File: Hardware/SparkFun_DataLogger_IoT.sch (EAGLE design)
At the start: 99 parts, among them J10 QWIIC_RIGHT_ANGLE, J3 MICRO-SD-PUSH-PUSH-EXT-PIN, J4 Vertical Qwiic Connector, U1 ESP-WROOM-32E, U10 74HC4066_QUAD_BILATERAL_SWITC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, U2 CH340C, U3 XC6222B331MR-G, U4 MAX17048, U5 MCP73831, U6 XC6222B331MR-G, U9 74HC4066_QUAD_BILATERAL_SWITC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

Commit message: Pre-Design Review updates
Add 9.1k Res for hardware versioning.
Move MEAS to be on grid.
Shuffle diodes around a little.
Move silk to fill gaps.
Change LED bias resistor to meet standards.
Made HW versioning be on A7 to match RTK designs.
Replaced A7 breakout with D5.
Relabeled silk.
Added silk to RGB LED.
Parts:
- removed R20, R21: 100k, SparkFun-Resistors:100KOHM-0402T-1/16W-1%
- R17: value 1M -> 100k; device SparkFun-Resistors:1MOHM-0402T-1/16W-5% -> SparkFun-Resistors:100KOHM-0402T-1/16W-1%
- R6: value 1k -> 2.2k; device SparkFun-Resistors:1KOHM-0402T-1/16W-1% -> SparkFun-Resistors:2.2KOHM-0402T-1/16W-1%
- R9: value 93.1k -> 9.1K; device SparkFun-Resistors:93.1KOHM-0402-1/16W-1%(93.1KOHM) -> RA_RGB:9.1KOHM-0402T-1/16W-1%
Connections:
- removed net ESP34/A6: R17.2, R9.1, U1.IA34
- new net ESP5: J8.5, U1.CS3/IO5
- net 3.3V: no longer R20.2, R21.2
- net ESP18/SCK: no longer R20.1
- net ESP23/PICO: no longer R21.1
- net ESP35/A7: now also R17.2, R9.1; no longer J8.5
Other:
- note added: "v10 should read ~0.275V"
- note removed: "v10 should read ~0.281V"
- moved on the sheet: J6, R22

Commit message: Post design review updates.
Change BO silk for D5.
Remove unused PURs.
Clean up wire stubs.
Remove GND guard trace.
Add GND vias near switching vias.
Renumber Schematic.
Repanelize and pull together outer border.
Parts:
- removed C28, C29, C30: 2.2uF, SparkFun-Capacitors:2.2UF-0402_TIGHT-10V-10%-X5R
- removed C31: 0.1uF, SparkFun-Capacitors:0.1UF-0402T-6.3V-10%-X7R
- removed J10: QWIIC_RIGHT_ANGLE, SparkFun-Connectors:QWIIC_CONNECTORJS-1MM
- removed R22: 10k, SparkFun-Resistors:10KOHM-0402T-1/16W-1%
- removed U10, U9: 74HC4066_QUAD_BILATERAL_SWITCH_QFN, SparkFun-IC-Logic:74HC4066_QUAD_BILATERAL_SWITCH_QFN
- added C21, C22, C24: 2.2uF, SparkFun-Capacitors:2.2UF-0402_TIGHT-10V-10%-X5R
- added C23: 0.1uF, SparkFun-Capacitors:0.1UF-0402T-6.3V-10%-X7R
- added J9: (no value), SparkFun-Connectors:JST_2MM_MALE
- added R18: 2.2k, SparkFun-Resistors:2.2KOHM-0402T-1/16W-1%
- added U7: MAX17048, SparkFun-IC-Power:MAX17048DFN8
- added U8: XC6222B331MR-G, SparkFun-IC-Power:XC6222B331MR-G
- C10, C14, C27, C5: value 2.2uF -> 0.1uF; device SparkFun-Capacitors:2.2UF-0402_TIGHT-10V-10%-X5R -> SparkFun-Capacitors:0.1UF-0402T-6.3V-10%-X7R
- C12: value 2.2uF -> 10nF; device SparkFun-Capacitors:2.2UF-0402_TIGHT-10V-10%-X5R -> SparkFun-Capacitors:10NF-0402T-25V-10%-X7R-WE
- C13, C15, C17, C19: value 0.1uF -> 2.2uF; device SparkFun-Capacitors:0.1UF-0402T-6.3V-10%-X7R -> SparkFun-Capacitors:2.2UF-0402_TIGHT-10V-10%-X5R
- C4: value 10nF -> 2.2uF; device SparkFun-Capacitors:10NF-0402T-25V-10%-X7R-WE -> SparkFun-Capacitors:2.2UF-0402_TIGHT-10V-10%-X5R
- D1: value BLUE -> 3A/10V/280mV; device SparkFun-LED:LED-BLUE0603 -> SparkFun-DiscreteSemi:DIODE-SCHOTTKY-BAT60A
- D2: value B3DQ3BRG -> 3A/10V/280mV; device RA_RGB:B3DQ3BRG -> SparkFun-DiscreteSemi:DIODE-SCHOTTKY-BAT60A
- D3: value Yellow -> 3A/10V/280mV; device SparkFun-LED:LED-YELLOW0603 -> SparkFun-DiscreteSemi:DIODE-SCHOTTKY-BAT60A
- D4: value 3A/10V/280mV -> TVS; device SparkFun-DiscreteSemi:DIODE-SCHOTTKY-BAT60A -> SparkFun-DiscreteSemi:DIODE_TVS
- D5: value 3A/10V/280mV -> Yellow; device SparkFun-DiscreteSemi:DIODE-SCHOTTKY-BAT60A -> SparkFun-LED:LED-YELLOW0603
- D6: value 3A/10V/280mV -> B3DQ3BRG; device SparkFun-DiscreteSemi:DIODE-SCHOTTKY-BAT60A -> RA_RGB:B3DQ3BRG
- D7: value TVS -> BLUE; device SparkFun-DiscreteSemi:DIODE_TVS -> SparkFun-LED:LED-BLUE0603
- J1: value (none) -> MICRO-SD-PUSH-PUSH-EXT-PIN; device SparkFun-Connectors:USB_C_4-LAYER_PADS -> SparkFun-Connectors:MICRO-SD-PUSH-PUSH-EXT-PIN
- J2: device SparkFun-Connectors:JST_2MM_MALE -> SparkFun-Connectors:CONN_06NO_SILK_NO_POP
- J3: value MICRO-SD-PUSH-PUSH-EXT-PIN -> QWIIC_RIGHT_ANGLE; device SparkFun-Connectors:MICRO-SD-PUSH-PUSH-EXT-PIN -> SparkFun-Connectors:QWIIC_CONNECTORJS-1MM
- J4: value Vertical Qwiic Connector -> (none); device SparkFun-Connectors:QWIIC_CONNECTOR -> SparkFun-Connectors:USB_C_4-LAYER_PADS
- J5: device SparkFun-Connectors:I2C_STANDARD_NO_SILK -> SparkFun-Connectors:CONN_041X04_NO_SILK_NO_POP
- J6: value (none) -> Vertical Qwiic Connector; device SparkFun-Connectors:CONN_041X04_NO_SILK_NO_POP -> SparkFun-Connectors:QWIIC_CONNECTOR
- J7: device SparkFun-Connectors:CONN_06NO_SILK_NO_POP -> SparkFun-Connectors:CONN_09NO_SILK
- J8: device SparkFun-Connectors:CONN_09NO_SILK -> SparkFun-Connectors:I2C_STANDARD_NO_SILK
- LOGO1: value SPECIAL_INSTRUCTIONS-ORDERING -> SFE_LOGO_NAME.2_INCH; device SparkFun-Aesthetics:SPECIAL_INSTRUCTIONS-ORDERING -> SparkFun-Aesthetics:SFE_LOGO_NAME.2_INCH
- LOGO3: value QWIIC_LOGO_6MM -> SPECIAL_INSTRUCTIONS-ORDERING; device SparkFun-Aesthetics:QWIIC_LOGO_6MM -> SparkFun-Aesthetics:SPECIAL_INSTRUCTIONS-ORDERING
- LOGO4: value OSHW-LOGOS -> QWIIC_LOGO_6MM; device SparkFun-Aesthetics:OSHW-LOGOS -> SparkFun-Aesthetics:QWIIC_LOGO_6MM
- LOGO5: value SFE_LOGO_NAME.2_INCH -> OSHW-LOGOS; device SparkFun-Aesthetics:SFE_LOGO_NAME.2_INCH -> SparkFun-Aesthetics:OSHW-LOGOS
- R1, R2: value 5.1k -> 10k; device SparkFun-Resistors:5.1KOHM-0402T-1/16W-1% -> SparkFun-Resistors:10KOHM-0402T-1/16W-1%
- R13: value 10k -> 1k; device SparkFun-Resistors:10KOHM-0402T-1/16W-1% -> SparkFun-Resistors:1KOHM-0402T-1/16W-1%
- R14: value 10k -> 2.0K; device SparkFun-Resistors:10KOHM-0402T-1/16W-1% -> SparkFun-Resistors:2.0KOHM-0402T-1/16W-1%
- R15: value 10k -> 2.2k; device SparkFun-Resistors:10KOHM-0402T-1/16W-1% -> SparkFun-Resistors:2.2KOHM-0402T-1/16W-1%
- R16: value 2.2k -> 100k; device SparkFun-Resistors:2.2KOHM-0402T-1/16W-1% -> SparkFun-Resistors:100KOHM-0402T-1/16W-1%
- R17: value 100k -> 9.1K; device SparkFun-Resistors:100KOHM-0402T-1/16W-1% -> RA_RGB:9.1KOHM-0402T-1/16W-1%
- R6: value 2.2k -> 10k; device SparkFun-Resistors:2.2KOHM-0402T-1/16W-1% -> SparkFun-Resistors:10KOHM-0402T-1/16W-1%
- R7: value 2.0K -> 10k; device SparkFun-Resistors:2.0KOHM-0402T-1/16W-1% -> SparkFun-Resistors:10KOHM-0402T-1/16W-1%
- R8: value 1k -> 5.1k; device SparkFun-Resistors:1KOHM-0402T-1/16W-1% -> SparkFun-Resistors:5.1KOHM-0402T-1/16W-1%
- R9: value 9.1K -> 5.1k; device RA_RGB:9.1KOHM-0402T-1/16W-1% -> SparkFun-Resistors:5.1KOHM-0402T-1/16W-1%
- U2: value CH340C -> 74HC4066_QUAD_BILATERAL_SWITCH_QFN; device SparkFun-IC-Comms:CH340C -> SparkFun-IC-Logic:74HC4066_QUAD_BILATERAL_SWITCH_QFN
- U4: value MAX17048 -> CH340C; device SparkFun-IC-Power:MAX17048DFN8 -> SparkFun-IC-Comms:CH340C
- U6: value XC6222B331MR-G -> 74HC4066_QUAD_BILATERAL_SWITCH_QFN; device SparkFun-IC-Power:XC6222B331MR-G -> SparkFun-IC-Logic:74HC4066_QUAD_BILATERAL_SWITCH_QFN
- renumbered LOGO6 to LOGO2, PWREN to TP4, VIN to TP2, VIN1 to TP3
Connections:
- net !RESET!: now also C5.1, J7.9, R1.1, U2.4E; no longer C31.1, J8.9, R3.1, U9.4E
- net 3.3V: now also C11.1, C12.1, C13.1, C17.1, C18.1, C6.1, C7.1, J2.5, R1.2, R10.2, R16.1, U3.OUT, U4.V3, U4.VCC, U6.VCC; no longer C1.1, C15.1, C2.1, C25.1, C26.1, C27.1, C28.1, J7.5, R17.1, R22.2, R3.2, U10.VCC, U2.V3, U6.OUT, U9.VCC
- net 3.3V_SW: now also C1.1, C2.1, C25.1, C26.1, C27.1, C8.1, D6.VCC, J1.VCC, J3.2, J6.2, J8.2, R2.2, R3.2, R4.2, R5.2, R6.2, U8.OUT; no longer C18.1, C19.1, C20.1, C5.1, C6.1, C7.1, D2.VCC, J10.2, J3.VCC, J4.2, J5.2, R10.2, R11.2, R12.2, R13.2, R14.2, U3.OUT
- net 5V: now also D3.A, J2.3; no longer D6.A, J7.3
- net CH340-DTR: now also R11.2, U4.!DTR; no longer R4.2, U2.!DTR
- net CH340-RTS: now also R12.2, U4.!RTS; no longer R5.2, U2.!RTS
- net CH340-RX: now also U4.RXI; no longer U2.RXI
- net CH340-TX: now also U4.TXO; no longer U2.TXO
- net D+: now also J4.D+, U4.UD+; no longer J1.D+, U2.UD+
- net D-: now also J4.D-, U4.UD-; no longer J1.D-, U2.UD-
- net ESP0/!BOOT!: now also J7.8; no longer J8.8
- net ESP12/DAT2: now also U2.2Y; no longer U9.2Y
- net ESP13/DAT3: now also J1.DAT3/!CS!, R2.1; no longer J3.DAT3/!CS!, R14.1
- net ESP14/CLK: now also J1.CLK/SCK; no longer J3.CLK/SCK
- net ESP15/CMD: now also U2.3Y; no longer U9.3Y
- net ESP16/RXD: now also J7.3; no longer J8.3
- net ESP17/TXD: now also J7.4; no longer J8.4
- net ESP18/SCK: now also J5.4; no longer J6.4
- net ESP19/POCI: now also J5.2, R10.1; no longer J6.2, R22.1
- net ESP2/DAT0: now also U2.1Y; no longer U9.1Y
- net ESP21/SDA: now also R15.1, U6.2Y, U7.SDA; no longer R19.1, U10.2Y, U4.SDA
- net ESP22/SCL: now also R18.2, U6.4Y, U7.SCL; no longer R16.2, U10.4Y, U4.SCL
- net ESP23/PICO: now also J5.3; no longer J6.3
- net ESP25/LED: now also J7.2, R19.2; no longer J8.2, R6.2
- net ESP26/RGBLED: now also J7.1; no longer J8.1
- net ESP32/PWREN: now also U2.4Y; no longer U9.4Y
- net ESP33: now also J5.1; no longer J6.1
- net ESP35/A7: now also R16.2, R17.1; no longer R17.2, R9.1
- net ESP36/A0: now also J7.7; no longer J8.7
- net ESP39/A3: now also J7.6; no longer J8.6
- net ESP4/DAT1: now also J1.DAT1, R4.1; no longer J3.DAT1, R12.1
- net ESP5: now also J7.5; no longer J8.5
- net GND: now also C21.2, C22.2, C23.2, C24.2, D4.A, D6.GND, D7.C, J2.2, J2.4, J2.6, J3.1, J4.GND, J6.1, J8.1, J9.-, R14.1, R17.2, R8.1, R9.1, U6.1E, U6.3E, U7.CTG, U7.GND, U7.QSTRT, U8.GND; no longer C28.2, C29.2, C30.2, C31.2, D1.C, D2.GND, D7.A, J10.1, J2.-, J3.GND, J4.1, J5.1, J7.2, J7.4, J7.6, R1.1, R15.1, R2.1, R9.2, U10.1E, U10.3E, U10.GND, U4.CTG, U4.QSTRT, U9.GND
- net N$1: now also J4.CC2, R8.2; no longer J1.CC2, R1.2
- net N$10: now also R13.2; no longer R8.2
- net N$11: now also R14.2; no longer R7.2
- net N$12: now also D6.DI; no longer D2.DI
- net N$13: now also D7.A; no longer D1.A
- net N$16: now also R18.1; no longer R16.1
- net N$17: now also R15.2; no longer R19.2
- net N$2: now also J4.CC1, R9.2; no longer J1.CC1, R2.2
- net N$3: now also D1.C, D2.C, D3.C; no longer D4.C, D5.C, D6.C
- net N$4: now also R12.1; no longer R5.1
- net N$5: now also R11.1; no longer R4.1
- net N$6: now also R19.1; no longer R6.1
- net N$7: now also D6.DO; no longer D2.DO
- net N$8: now also D5.A; no longer D3.A
- net N$9: now also D5.C, R13.1; no longer D3.C, R8.1
- net PWREN: now also R7.2, U2.1E, U2.2E, U2.3E, U2.4Z, U6.2E, U6.4E, U8.EN; no longer R15.2, U10.2E, U10.4E, U3.EN, U9.1E, U9.2E, U9.3E, U9.4Z
- net QWIIC_SCL: now also J3.4, J6.4, J8.4, U6.4Z; no longer J10.4, J4.4, J5.4, U10.4Z
- net QWIIC_SDA: now also J3.3, J6.3, J8.3, U6.2Z; no longer J10.3, J4.3, J5.3, U10.2Z
- net SD_CMD: now also J1.CMD/SDI, R6.1, U2.3Z; no longer J3.CMD/SDI, R10.1, U9.3Z
- net SD_DAT0: now also J1.DAT0/SDO, R5.1, U2.1Z; no longer J3.DAT0/SDO, R11.1, U9.1Z
- net SD_DAT2: now also J1.DAT2, R3.1, U2.2Z; no longer J3.DAT2, R13.1, U9.2Z
- net SHIELD: now also J4.SHLD; no longer J1.SHLD
- net VIN: now also C15.1, C19.1, C21.1, C22.1, C24.1, U3.EN, U8.IN; no longer C12.1, C16.1, C17.1, C29.1, C8.1, U6.EN, U6.IN
- net V_BATT: now also C16.1, C20.1, C23.1, D1.A, J2.1, J9.+, U7.CELL, U7.VDD; no longer C11.1, C13.1, C30.1, D4.A, J2.+, J7.1, U4.CELL, U4.VDD
- net V_USB: now also D2.A, D4.C, J4.VBUS; no longer D5.A, D7.C, J1.VBUS
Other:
- note added: "TP2"
- note added: "TP3"
- note added: "TP4"
- note removed: "Close jumper to connect INT to ESP35"
- moved on the sheet: C1, C10, C11, C12, C13, C14, C15, C16, C17, C18, C19, C2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

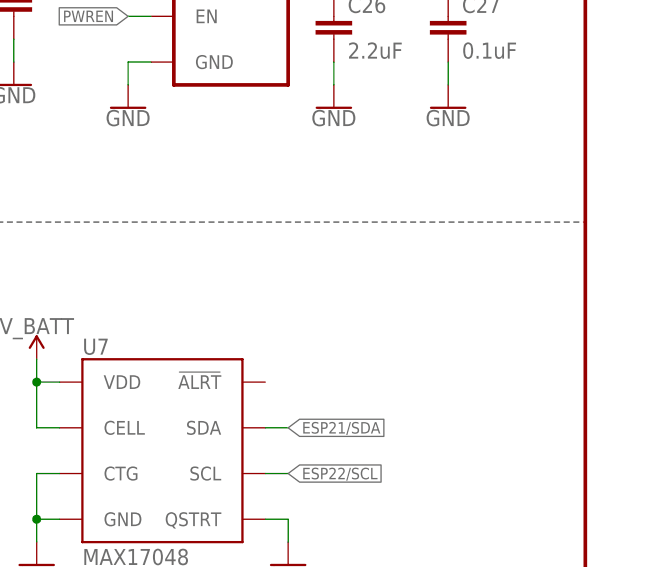
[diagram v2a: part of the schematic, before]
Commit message: Added Fuel Gauge I2C address.
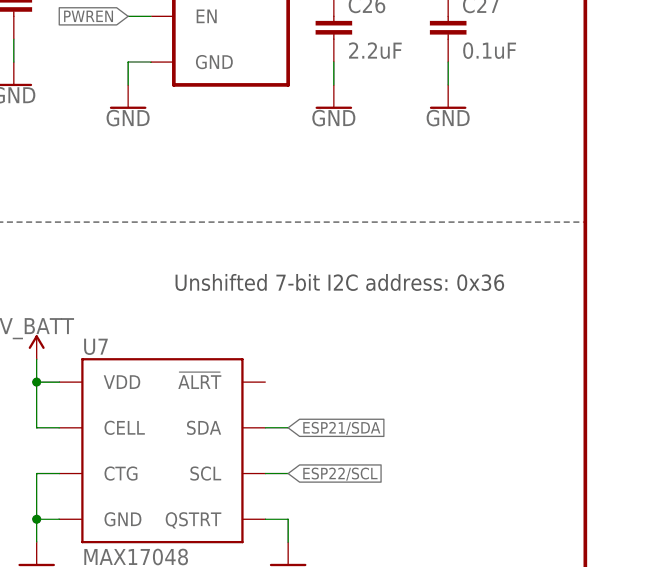
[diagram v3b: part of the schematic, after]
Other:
- note added: "Unshifted 7-bit I2C address: 0x36"
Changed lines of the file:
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@@
 <text x="264.16" y="147.32" size="1.778" layer="95" font="vector">TP3</text>
 <text x="81.28" y="43.18" size="1.778" layer="95" font="vector">TP4</text>
+<text x="386.08" y="167.64" size="1.778" layer="97" font="vector">Unshifted 7-bit I2C address: 0x36</text>
 </plain>
 <instances>

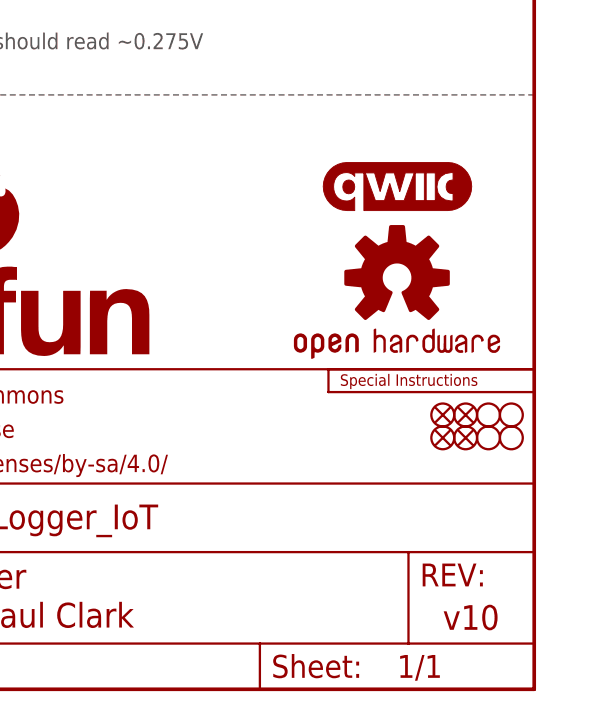
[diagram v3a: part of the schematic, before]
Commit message: Update for v11 PCB
Removed OSHW logo.
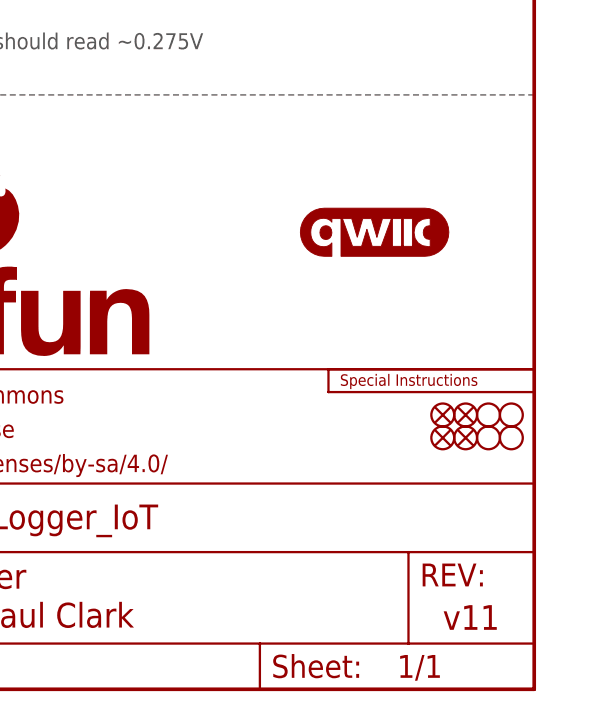
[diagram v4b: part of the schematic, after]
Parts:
- removed LOGO5: OSHW-LOGOS, SparkFun-Aesthetics:OSHW-LOGOS
- FRAME1: REV v10 -> v11
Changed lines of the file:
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@@
 <part name="FRAME1" library="SparkFun-Aesthetics" deviceset="FRAME-LEDGER" device="">
 <attribute name="DESIGNER" value="Alex Brudner"/>
-<attribute name="REV" value="v10"/>
+<attribute name="REV" value="v11"/>
 </part>
 <part name="LOGO3" library="SparkFun-Aesthetics" deviceset="SPECIAL_INSTRUCTIONS" device="-ORDERING"/>
@@
 <part name="H1" library="SparkFun-Hardware" deviceset="STAND-OFF" device="TIGHT"/>
 <part name="LOGO4" library="SparkFun-Aesthetics" deviceset="QWIIC_LOGO" device="_6MM" value="QWIIC_LOGO_6MM"/>
-<part name="LOGO5" library="SparkFun-Aesthetics" deviceset="OSHW-LOGO" device="S" value="OSHW-LOGOS"/>
 <part name="SUPPLY7" library="SparkFun-PowerSymbols" deviceset="V_USB" device=""/>
 <part name="GND10" library="SparkFun-PowerSymbols" deviceset="GND" device=""/>
@@
 </instance>
 <instance part="H1" gate="G$1" x="426.72" y="30.48" smashed="yes"/>
-<instance part="LOGO4" gate="G$1" x="416.56" y="55.88" smashed="yes"/>
-<instance part="LOGO5" gate="G$1" x="416.56" y="45.72" smashed="yes"/>
+<instance part="LOGO4" gate="G$1" x="414.02" y="50.8" smashed="yes"/>
 <instance part="SUPPLY7" gate="G$1" x="149.86" y="228.6" smashed="yes">
 <attribute name="VALUE" x="149.86" y="231.394" size="1.778" layer="96" align="bottom-center"/>

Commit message: Condensed Schematic.
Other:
- note removed: "HW Versioning"
- note removed: "v10 should read ~0.275V"
- moved on the sheet: R16, R17
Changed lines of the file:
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@@
 <text x="106.68" y="35.56" size="2.54" layer="94" font="vector">Qwiic Connectors</text>
 <wire x1="99.06" y1="43.18" x2="99.06" y2="0" width="0.1524" layer="97" style="longdash"/>
-<wire x1="330.2" y1="35.56" x2="330.2" y2="66.04" width="0.1524" layer="97" style="longdash"/>
-<wire x1="330.2" y1="66.04" x2="330.2" y2="106.68" width="0.1524" layer="97" style="longdash"/>
+<wire x1="330.2" y1="35.56" x2="330.2" y2="106.68" width="0.1524" layer="97" style="longdash"/>
 <wire x1="223.52" y1="106.68" x2="223.52" y2="43.18" width="0.1524" layer="97" style="longdash"/>
 <wire x1="223.52" y1="43.18" x2="223.52" y2="0" width="0.1524" layer="97" style="longdash"/>
-<text x="337.82" y="99.06" size="2.54" layer="94" font="vector">HW Versioning</text>
-<wire x1="431.8" y1="66.04" x2="330.2" y2="66.04" width="0.1524" layer="97" style="longdash"/>
-<text x="381" y="71.12" size="1.778" layer="97" font="vector" align="bottom-center">v10 should read ~0.275V</text>
 <text x="165.1" y="142.24" size="1.778" layer="95" font="vector">TP2</text>
 <text x="264.16" y="147.32" size="1.778" layer="95" font="vector">TP3</text>
@@
 </instance>
 <instance part="H1" gate="G$1" x="426.72" y="30.48" smashed="yes"/>
-<instance part="LOGO4" gate="G$1" x="414.02" y="50.8" smashed="yes"/>
+<instance part="LOGO4" gate="G$1" x="414.02" y="43.18" smashed="yes"/>
 <instance part="SUPPLY7" gate="G$1" x="149.86" y="228.6" smashed="yes">
 <attribute name="VALUE" x="149.86" y="231.394" size="1.778" layer="96" align="bottom-center"/>
@@
 <instance part="LOGO1" gate="G$1" x="332.74" y="33.02" smashed="yes"/>
 <instance part="LOGO2" gate="G$1" x="365.76" y="44.45" smashed="yes"/>
-<instance part="R17" gate="G$1" x="388.62" y="86.36" smashed="yes">
-<attribute name="NAME" x="388.62" y="87.884" size="1.778" layer="95" font="vector" align="bottom-center"/>
-<attribute name="VALUE" x="388.62" y="84.836" size="1.778" layer="96" font="vector" align="top-center"/>
-</instance>
-<instance part="R16" gate="G$1" x="373.38" y="86.36" smashed="yes">
-<attribute name="NAME" x="373.38" y="87.884" size="1.778" layer="95" font="vector" align="bottom-center"/>
-<attribute name="VALUE" x="373.38" y="84.836" size="1.778" layer="96" font="vector" align="top-center"/>
-</instance>
-<instance part="SUPPLY31" gate="G$1" x="365.76" y="88.9" smashed="yes">
-<attribute name="VALUE" x="365.76" y="91.694" size="1.778" layer="96" align="bottom-center"/>
-</instance>
-<instance part="GND36" gate="1" x="396.24" y="81.28" smashed="yes">
-<attribute name="VALUE" x="396.24" y="81.026" size="1.778" layer="96" font="vector" align="top-center"/>
+<instance part="R17" gate="G$1" x="86.36" y="193.04" smashed="yes" rot="R270">
+<attribute name="NAME" x="87.884" y="193.04" size="1.778" layer="95" font="vector" rot="R270" align="bottom-center"/>
+<attribute name="VALUE" x="92.456" y="193.04" size="1.778" layer="96" font="vector" rot="R270" align="top-center"/>
+</instance>
+<instance part="R16" gate="G$1" x="86.36" y="208.28" smashed="yes" rot="R270">
+<attribute name="NAME" x="87.884" y="208.28" size="1.778" layer="95" font="vector" rot="R270" align="bottom-center"/>
+<attribute name="VALUE" x="92.456" y="208.28" size="1.778" layer="96" font="vector" rot="R270" align="top-center"/>
+</instance>
+<instance part="SUPPLY31" gate="G$1" x="86.36" y="215.9" smashed="yes">
+<attribute name="VALUE" x="86.36" y="218.694" size="1.778" layer="96" align="bottom-center"/>
+</instance>
+<instance part="GND36" gate="1" x="86.36" y="182.88" smashed="yes">
+<attribute name="VALUE" x="86.36" y="182.626" size="1.778" layer="96" font="vector" align="top-center"/>
 </instance>
 <instance part="MEAS" gate="JP1" x="139.7" y="139.7" smashed="yes">
@@
 </segment>
 <segment>
-<wire x1="393.7" y1="86.36" x2="396.24" y2="86.36" width="0.1524" layer="91"/>
 <pinref part="GND36" gate="1" pin="GND"/>
-<wire x1="396.24" y1="86.36" x2="396.24" y2="83.82" width="0.1524" layer="91"/>
+<wire x1="86.36" y1="187.96" x2="86.36" y2="185.42" width="0.1524" layer="91"/>
 <pinref part="R17" gate="G$1" pin="2"/>
 </segment>
@@
 <segment>
 <pinref part="SUPPLY31" gate="G$1" pin="3.3V"/>
-<wire x1="365.76" y1="86.36" x2="365.76" y2="88.9" width="0.1524" layer="91"/>
 <pinref part="R16" gate="G$1" pin="1"/>
-<wire x1="368.3" y1="86.36" x2="365.76" y2="86.36" width="0.1524" layer="91" style="longdash"/>
+<wire x1="86.36" y1="213.36" x2="86.36" y2="215.9" width="0.1524" layer="91"/>
 </segment>
 </net>
@@
 <net name="ESP35/A7" class="0">
 <segment>
-<pinref part="U1" gate="U1" pin="IA35"/>
-<wire x1="66.04" y1="200.66" x2="68.58" y2="200.66" width="0.1524" layer="91"/>
-<label x="68.58" y="200.66" size="1.27" layer="95" font="vector" xref="yes"/>
-</segment>
-<segment>
 <pinref part="R17" gate="G$1" pin="1"/>
 <pinref part="R16" gate="G$1" pin="2"/>
-<wire x1="383.54" y1="86.36" x2="381" y2="86.36" width="0.1524" layer="91"/>
-<wire x1="381" y1="86.36" x2="378.46" y2="86.36" width="0.1524" layer="91"/>
-<wire x1="381" y1="86.36" x2="381" y2="78.74" width="0.1524" layer="91"/>
-<wire x1="381" y1="78.74" x2="378.46" y2="78.74" width="0.1524" layer="91"/>
-<junction x="381" y="86.36"/>
-<label x="378.46" y="78.74" size="1.27" layer="95" font="vector" rot="R180" xref="yes"/>
-</segment>
-</net>
+<wire x1="86.36" y1="198.12" x2="86.36" y2="200.66" width="0.1524" layer="91"/>
+<wire x1="86.36" y1="200.66" x2="86.36" y2="203.2" width="0.1524" layer="91"/>
+<wire x1="86.36" y1="200.66" x2="81.28" y2="200.66" width="0.1524" layer="91"/>
+<wire x1="81.28" y1="200.66" x2="81.28" y2="198.12" width="0.1524" layer="91"/>
+<junction x="86.36" y="200.66"/>
+<label x="81.28" y="198.12" size="1.27" layer="95" font="vector" rot="R270" xref="yes"/>
+<pinref part="U1" gate="U1" pin="IA35"/>
+<wire x1="81.28" y1="200.66" x2="66.04" y2="200.66" width="0.1524" layer="91"/>
+<junction x="81.28" y="200.66"/>
+</segment>
+</net>

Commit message: NP unused resistors
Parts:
- R16: value 100k -> DNP; device SparkFun-Resistors:100KOHM-0402T-1/16W-1% -> SparkFun-Resistors:DNP-0402T_NO_CREAM
- R17: value 9.1K -> DNP; device RA_RGB:9.1KOHM-0402T-1/16W-1% -> SparkFun-Resistors:DNP-0402T_NO_CREAM
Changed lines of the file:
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@@
 <part name="LOGO1" library="SparkFun-Aesthetics" deviceset="SFE_LOGO_NAME" device=".2_INCH"/>
 <part name="LOGO2" library="SparkFun-Aesthetics" deviceset="SFE_LOGO_FLAME" device=".2_INCH"/>
-<part name="R17" library="RA_RGB" deviceset="9.1KOHM" device="-0402T-1/16W-1%" value="9.1K"/>
-<part name="R16" library="SparkFun-Resistors" deviceset="100KOHM" device="-0402T-1/16W-1%" value="100k"/>
+<part name="R17" library="SparkFun-Resistors" deviceset="DNP" device="-0402T_NO_CREAM" value="DNP"/>
+<part name="R16" library="SparkFun-Resistors" deviceset="DNP" device="-0402T_NO_CREAM" value="DNP"/>
 <part name="SUPPLY31" library="SparkFun-PowerSymbols" deviceset="3.3V" device=""/>
 <part name="GND36" library="SparkFun-PowerSymbols" deviceset="GND" device=""/>

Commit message: Update VREG
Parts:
- U3, U8: value XC6222B331MR-G -> 3.3V; device SparkFun-IC-Power:XC6222B331MR-G -> SparkFun-IC-Power:V_REG_AP2112K-3.3V
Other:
- note added: "Vin Max: 6.0V Iout Max: 600mA Vdo: 250mV @ 600mA Output Discharge: 60Ω Typ"
- note removed: "Vin Max: 6.0V Iout Max: 700mA Vdo: 120mV @ 330mA Output Discharge: 530Ω Typ"
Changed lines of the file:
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@@
 <part name="C25" library="SparkFun-Capacitors" deviceset="2.2UF" device="-0402_TIGHT-10V-10%-X5R" value="2.2uF"/>
 <part name="GND16" library="SparkFun-PowerSymbols" deviceset="GND" device=""/>
-<part name="U8" library="SparkFun-IC-Power" deviceset="XC6222" device="B331MR-G" value="XC6222B331MR-G"/>
+<part name="U8" library="SparkFun-IC-Power" deviceset="V_REG_AP2112" device="K-3.3V" value="3.3V"/>
 <part name="GND17" library="SparkFun-PowerSymbols" deviceset="GND" device=""/>
 <part name="SUPPLY11" library="SparkFun-PowerSymbols" deviceset="3.3V_SW" device=""/>
@@
 <part name="SUPPLY20" library="SparkFun-PowerSymbols" deviceset="V_BATT" device=""/>
 <part name="GND30" library="SparkFun-PowerSymbols" deviceset="GND" device=""/>
-<part name="U3" library="SparkFun-IC-Power" deviceset="XC6222" device="B331MR-G" value="XC6222B331MR-G"/>
+<part name="U3" library="SparkFun-IC-Power" deviceset="V_REG_AP2112" device="K-3.3V" value="3.3V"/>
 <part name="C13" library="SparkFun-Capacitors" deviceset="2.2UF" device="-0402_TIGHT-10V-10%-X5R" value="2.2uF"/>
 <part name="C14" library="SparkFun-Capacitors" deviceset="0.1UF" device="-0402T-6.3V-10%-X7R" value="0.1uF"/>
@@
 <text x="48.006" y="272.034" size="1.778" layer="97" font="vector" align="top-center">VDD Range: 3.0V - 3.6V</text>
 <text x="172.466" y="150.114" size="1.778" layer="97" font="vector">Vin Max: 6.0V
-Iout Max: 700mA
-Vdo: 120mV @ 330mA
-Output Discharge: 530Ω Typ</text>
+Iout Max: 600mA
+Vdo: 250mV @ 600mA
+Output Discharge: 60Ω Typ</text>
 <text x="276.86" y="185.42" size="1.778" layer="97" font="vector" align="top-center">If DTR is LOW, toggling RTS from HIGH to LOW resets to run mode.
 If RTS is HIGH, toggling DTR from LOW to HIGH resets to bootloader.</text>
@@
 <wire x1="254" y1="127" x2="255.27" y2="125.73" width="0.1524" layer="97"/>
 <text x="385.826" y="213.614" size="1.778" layer="97" font="vector">Vin Max: 6.0V
-Iout Max: 700mA
-Vdo: 120mV @ 330mA
-Output Discharge: 530Ω Typ</text>
+Iout Max: 600mA
+Vdo: 250mV @ 600mA
+Output Discharge: 60Ω Typ</text>
 <text x="331.724" y="6.858" size="2.7432" layer="94" font="vector">Based on a design by: Paul Clark</text>
 <text x="106.68" y="35.56" size="2.54" layer="94" font="vector">Qwiic Connectors</text>
